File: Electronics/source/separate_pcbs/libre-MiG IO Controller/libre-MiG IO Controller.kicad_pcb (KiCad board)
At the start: 2 copper layers, 60 x 34.4 mm, 30 parts, among them J10 Conn_01x03, J11 Conn_01x08, J12 Conn_01x08, J13 Conn_01x05, J14 Conn_01x03, J15 Conn_01x06, J8 Conn_01x03, J9 Conn_01x03, U2 TCA9535PWR, U3 TCA9535PWR, U6 MAX11615EEE

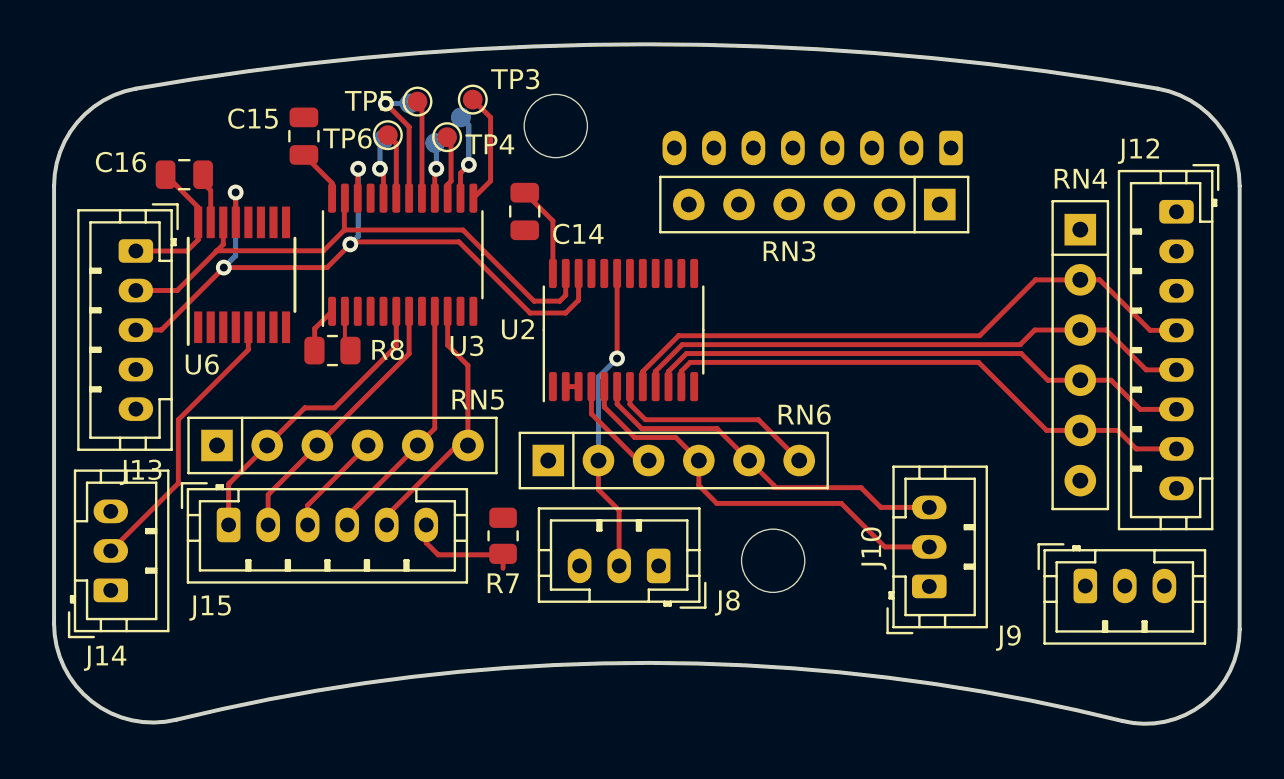
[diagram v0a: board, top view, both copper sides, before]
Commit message: added mechanical ignore
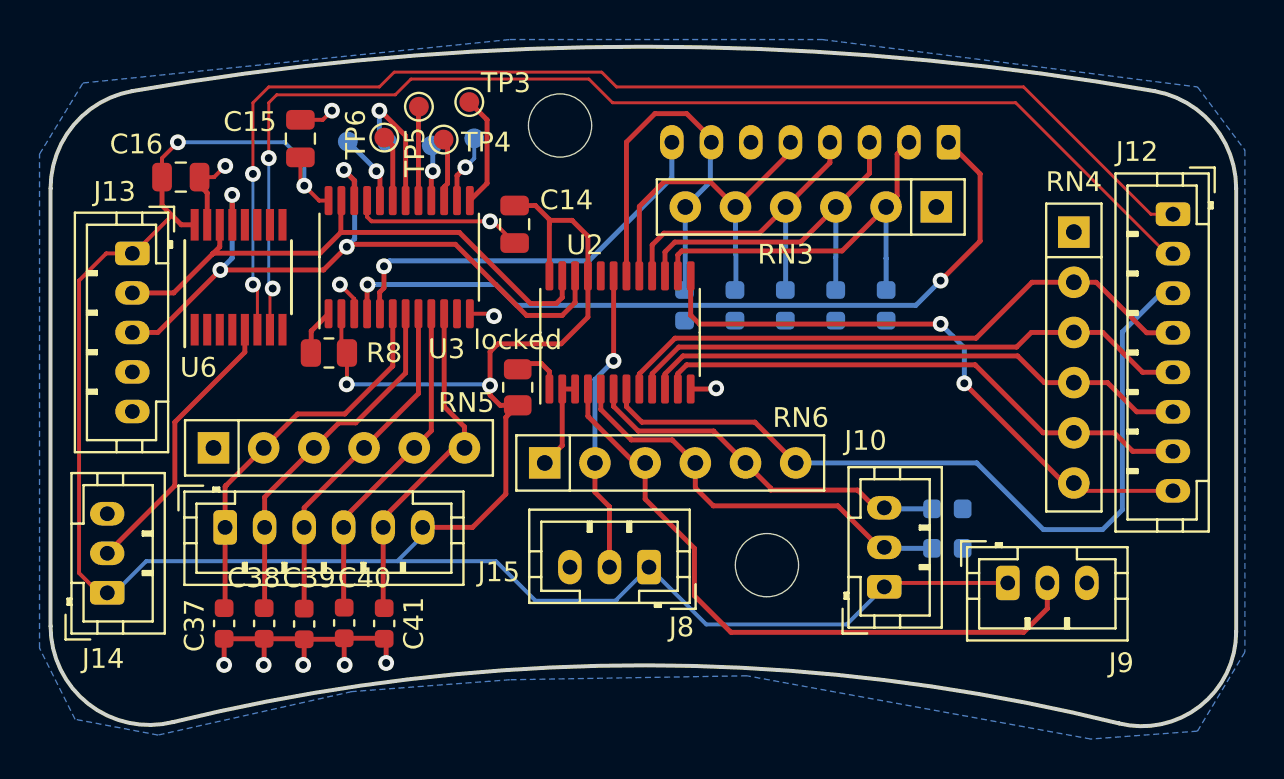
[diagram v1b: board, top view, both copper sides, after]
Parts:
- removed R7: 10k, Resistor_SMD:R_0805_2012Metric
- removed the REF** at (143.1, 181.6)
- removed the REF** at (132.0, 159.6)
- added C25: 100nF, Capacitor_SMD:C_0603_1608Metric, B.Cu at (143.7, 168.7)
- added C33: 100nF, Capacitor_SMD:C_0603_1608Metric, B.Cu at (146.2, 168.7)
- added C34: 100nF, Capacitor_SMD:C_0603_1608Metric, B.Cu at (141.1, 168.7)
- added C35: 100nF, Capacitor_SMD:C_0603_1608Metric, B.Cu at (138.6, 168.7)
- added C36: 100nF, Capacitor_SMD:C_0603_1608Metric, B.Cu at (148.8, 168.7)
- added C37: 100nF, Capacitor_SMD:C_0603_1608Metric, F.Cu at (115.2, 184.8)
- added C38: 100nF, Capacitor_SMD:C_0603_1608Metric, F.Cu at (117.3, 184.8)
- added C39: 100nF, Capacitor_SMD:C_0603_1608Metric, F.Cu at (119.3, 184.8)
- added C40: 100nF, Capacitor_SMD:C_0603_1608Metric, F.Cu at (121.3, 184.8)
- added C41: 100nF, Capacitor_SMD:C_0603_1608Metric, F.Cu at (123.3, 184.8)
- added C42: 100nF, Capacitor_SMD:C_0603_1608Metric, B.Cu at (151.8, 181.0)
- added C43: 100nF, Capacitor_SMD:C_0603_1608Metric, B.Cu at (151.8, 179.0)
- added REF**: MountingHole_3.2mm_M3, MountingHole:MountingHole_3.2mm_M3, F.Cu at (142.8, 181.8)
- added REF**: MountingHole_3.2mm_M3, MountingHole:MountingHole_3.2mm_M3, F.Cu at (132.2, 159.6)
- added locked: 10k, Resistor_SMD:R_0805_2012Metric, F.Cu at (130.1, 172.8)
- moved J9 3.93 mm to (154.9, 182.7)
- moved J10 2.28 mm to (148.7, 182.9)
- moved TP9 2.26 mm to (123.5, 160.4)
- moved TP10 1.83 mm to (121.5, 160.4)
- moved TP7 1.26 mm to (127.9, 160.2)
- moved C14 0.83 mm to (129.9, 164.6)
- moved J8 0.49 mm to (136.8, 181.9)
- moved RN4 0.35 mm to (158.2, 165.0)
- moved J11 0.32 mm to (151.9, 160.4)
- moved TP5 0.27 mm to (125.1, 158.6)
- moved C15 0.22 mm to (119.1, 160.3)
- moved J12 0.22 mm to (163.3, 164.1)
- moved J13 0.22 mm to (110.6, 166.1)
- moved J14 0.22 mm to (109.3, 183.2)
- moved RN6 0.22 mm to (131.5, 176.7)
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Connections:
- J11 pad 2: /IO Controller/EncodeB -> /IO Controller/DirU1
- J11 pad 3: /IO Controller/DirC1 -> /IO Controller/DirR1
- J11 pad 4: /IO Controller/DirR1 -> /IO Controller/DirC1
- J11 pad 6: /IO Controller/DirU1 -> GND
- J11 pad 8: GND -> /IO Controller/EncodeB
- RN3 pad 2: /IO Controller/DirC1 -> /IO Controller/DirU1
- RN3 pad 4: /IO Controller/DirL1 -> /IO Controller/DirC1
- RN3 pad 5: /IO Controller/DirU1 -> /IO Controller/DirL1
- U2 pad 14: /IO Controller/DirC1 -> /IO Controller/DirU1
- U2 pad 15: /IO Controller/DirL1 -> /IO Controller/DirR1
- U2 pad 16: /IO Controller/DirR1 -> /IO Controller/DirC1
- U2 pad 17: /IO Controller/DirU1 -> /IO Controller/DirL1
- U3 pad 8: /IO Controller/SideU -> /IO Controller/SideC
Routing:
- net +3V3: track 22.9 -> 133.0 mm, vias 0 -> 4
- net /IO Controller/Axis1: track 0.00 -> 61.8 mm, vias 0 -> 2
- net /IO Controller/Axis2: track 0.00 -> 61.5 mm, vias 0 -> 2
- net /IO Controller/EncodeA: track 0.00 -> 39.9 mm, vias 0 -> 2
- net GND: track 2.81 -> 37.8 mm, vias 0 -> 11
- net /IO Controller/DirD: track 0.00 -> 31.2 mm, vias 0 -> 2
- net /IO Controller/CenterButt: track 10.6 -> 41.4 mm
- net /IO Controller/BigRed: track 5.25 -> 33.4 mm
- net /IO Controller/EncodeB: track 0.00 -> 20.7 mm, vias 0 -> 1
- net /IO Controller/DirU1: track 0.00 -> 20.6 mm
- net /IO Controller/DirD1: track 0.00 -> 19.7 mm
- net /IO Controller/DirR1: track 0.00 -> 19.0 mm
- net /IO Controller/DirL1: track 0.00 -> 18.1 mm
- net /IO Controller/DirC1: track 0.00 -> 17.5 mm
- net /IO Controller/SideC: track 5.28 -> 17.3 mm
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- added copper zone on B.Cu, net GND
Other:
- board text added: "Conn_01x20"
